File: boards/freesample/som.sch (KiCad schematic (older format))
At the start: 15 parts, among them J10 XILINX_JTAG, J19 JUMPER, J20 JUMPER, J21 JUMPER, J7 CONN_INTEGRALSTICK_FPGA_HOST, J8 CONN_INTEGRALSTICK_MCU_HOST, J9 0826-1G1T-23-F, Q1 SSM6N58NU

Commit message: Added more test points. Started picking packages for passives. Continued schematic review.
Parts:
- added J24, J25: SMA, azonenberg_pcb:CONN_SMA_EDGE_SAMTEC_SMA_J_P_H_ST_EM1, symbol Connector:Conn_Coaxial
- C129, C130, C131, C132, C321: footprint (none) -> azonenberg_pcb:EIA_0402_CAP_NOSILK
- J10: footprint (none) -> azonenberg_pcb:XILINX_JTAG_PTH_MOLEX_0878311420
- J7, J8: footprint (none) -> azonenberg_pcb:CONN_SAMTEC_QSH-060-01-L-D-A
- J9: footprint (none) -> azonenberg_pcb:CONN_BELFUSE_0826_1G1T_23_F
- Q1: footprint (none) -> azonenberg_pcb:DFN_6_0.65MM_2x2MM_GDS
- R16, R17: footprint (none) -> azonenberg_pcb:EIA_0402_RES_NOSILK
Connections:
- net GND: now also J24.2 (Ext), J25.2 (Ext)
- net SMA_GPIO_N: now reaches J7.10 (LVDS_DQ8_N)
- net SMA_GPIO_N: now also J25.1 (In)
- net SMA_GPIO_P: now reaches J7.12 (LVDS_DQ8_P)
- net SMA_GPIO_P: now also J24.1 (In)
- no-connect marks 88 -> 86

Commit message: Continued assigning footprints
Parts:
- J19, J20, J21: footprint (none) -> azonenberg_pcb:CONN_HEADER_2.54MM_1x2
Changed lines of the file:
@@
 Sheet 9 12
 Title "FREESAMPLE Oscilloscope"
-Date "2019-03-15"
+Date "2019-03-16"
 Rev "0.1"
 Comp "Andrew D. Zonenberg / Antikernel Labs"
@@
 F 0 "J19" H 10130 5642 50  0000 L CNN
 F 1 "JUMPER" H 10130 5551 50  0000 L CNN
-F 2 "" H 10050 5650 50  0001 C CNN
+F 2 "azonenberg_pcb:CONN_HEADER_2.54MM_1x2" H 10050 5650 50  0001 C CNN
 F 3 "~" H 10050 5650 50  0001 C CNN
 	1    10050 5650
@@
 F 0 "J20" H 10130 5992 50  0000 L CNN
 F 1 "JUMPER" H 10130 5901 50  0000 L CNN
-F 2 "" H 10050 6000 50  0001 C CNN
+F 2 "azonenberg_pcb:CONN_HEADER_2.54MM_1x2" H 10050 6000 50  0001 C CNN
 F 3 "~" H 10050 6000 50  0001 C CNN
 	1    10050 6000
@@
 F 0 "J21" H 10130 6292 50  0000 L CNN
 F 1 "JUMPER" H 10130 6201 50  0000 L CNN
-F 2 "" H 10050 6300 50  0001 C CNN
+F 2 "azonenberg_pcb:CONN_HEADER_2.54MM_1x2" H 10050 6300 50  0001 C CNN
 F 3 "~" H 10050 6300 50  0001 C CNN
 	1    10050 6300

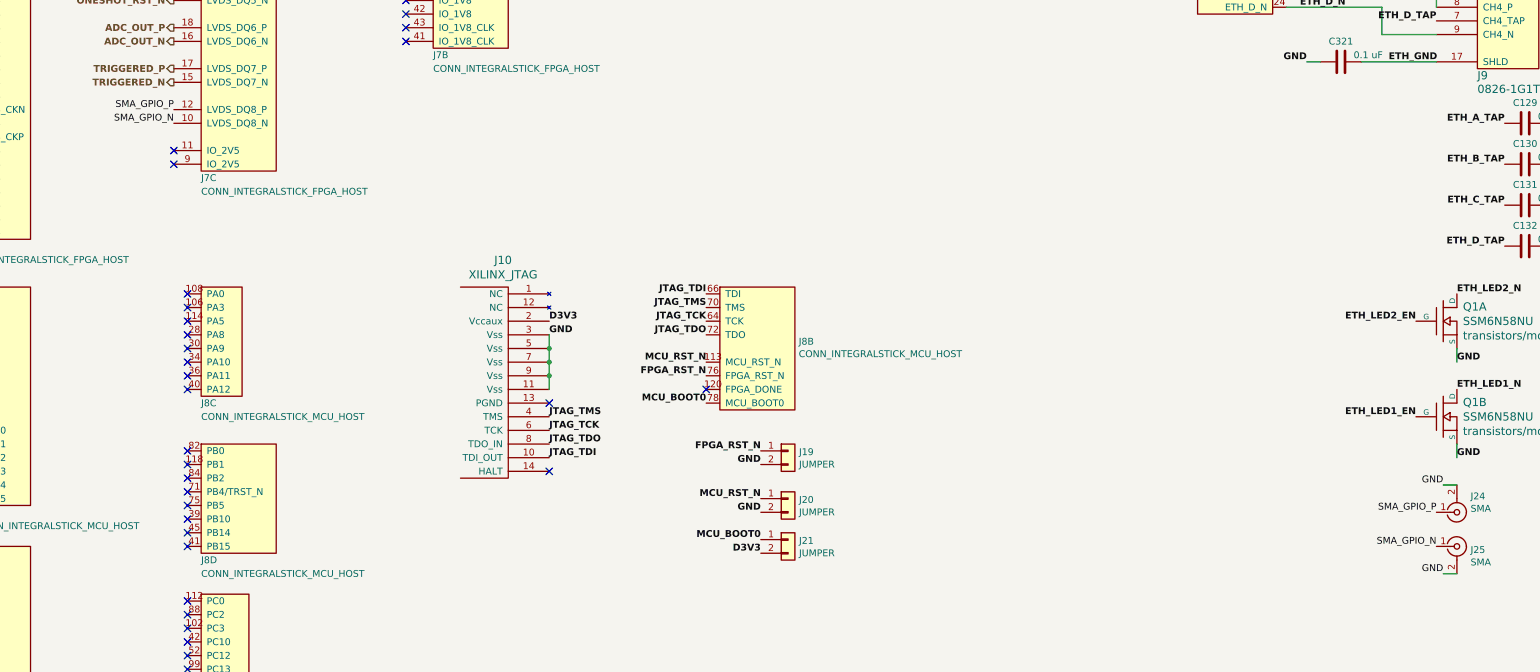
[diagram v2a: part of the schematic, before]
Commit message: Continued schematic review. Significantly simplified one-shot to reduce jitter, board area, and power consumption
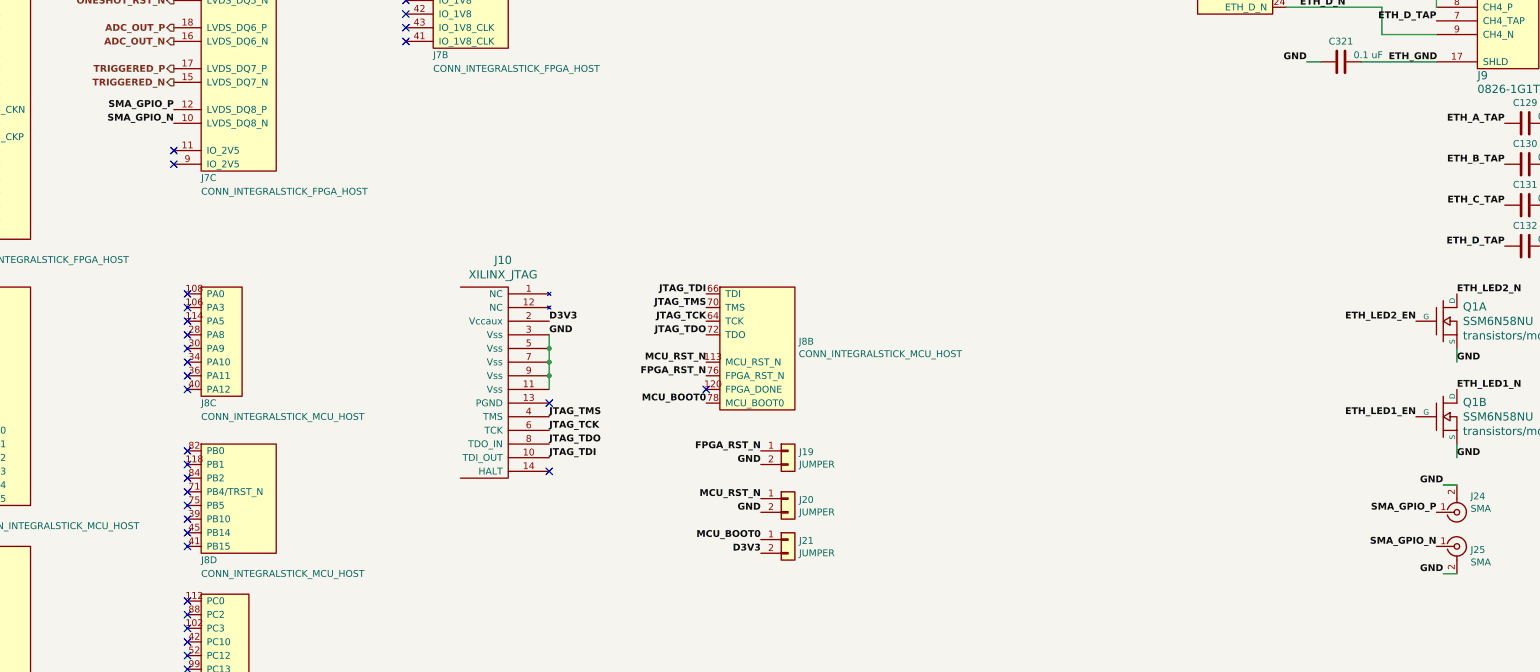
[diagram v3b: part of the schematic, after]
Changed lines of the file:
@@
 Text Label 9450 5300 2    50   ~ 6
 MCU_BOOT0
-Text Label 5550 3150 2    50   ~ 0
+Text Label 5550 3150 2    50   ~ 6
 SMA_GPIO_P
-Text Label 5550 3250 2    50   ~ 0
+Text Label 5550 3250 2    50   ~ 6
 SMA_GPIO_N
-Text Label 14800 6100 2    50   ~ 0
+Text Label 14800 6100 2    50   ~ 6
 SMA_GPIO_P
-Text Label 14800 6350 2    50   ~ 0
+Text Label 14800 6350 2    50   ~ 6
 SMA_GPIO_N
 $Comp
@@
 	1    0    0    -1
 $EndComp
-Text Label 14850 6550 2    50   ~ 0
+Text Label 14850 6550 2    50   ~ 6
 GND
 Wire Wire Line
 	14850 6550 14950 6550
-Text Label 14850 5900 2    50   ~ 0
+Text Label 14850 5900 2    50   ~ 6
 GND
 Wire Wire Line

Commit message: Finished schematic review. Added a bunch more test points. Need to make a few footprints then ready for layout!
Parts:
- added J26: PMOD_HOST, azonenberg_pcb:CONN_HEADER_2.54MM_2x6_RA_PMOD_HOST, symbol special-azonenberg:PMOD_HOST
- added TP32, TP33, TP34, TP35: GROUNDCLIP, azonenberg_pcb:TESTPOINT_SMT_KEYSTONE_5016, symbol Connector:Conn_01x01
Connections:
- net D3V3: now also J26.12 (3V3), J26.6 (3V3)
- net GND: now also J26.11 (GND), J26.5 (GND), TP32.1 (Pin_1), TP33.1 (Pin_1), TP34.1 (Pin_1), TP35.1 (Pin_1)
- net GPIO7: now reaches J7.104 (IO_3V3)
- net GPIO7: now also J26.10 (D7)
- net GPIO0: now reaches J7.110 (IO_3V3)
- net GPIO0: now also J26.1 (D0)
- net GPIO1: now reaches J7.113 (IO_3V3)
- net GPIO1: now also J26.2 (D1)
- net GPIO2: now reaches J7.114 (IO_3V3)
- net GPIO2: now also J26.3 (D2)
- net GPIO3: now reaches J7.115 (IO_3V3)
- net GPIO3: now also J26.4 (D3)
- net GPIO4: now reaches J7.116 (IO_3V3)
- net GPIO4: now also J26.7 (D4)
- net GPIO5: now reaches J7.119 (IO_3V3)
- net GPIO5: now also J26.8 (D5)
- net GPIO6: now reaches J7.120 (IO_3V3)
- net GPIO6: now also J26.9 (D6)
- no-connect marks 86 -> 78
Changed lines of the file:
@@
 	1    0    0    -1
 $EndComp
-NoConn ~ 3800 3050
 NoConn ~ 3800 3250
-NoConn ~ 3800 3450
-NoConn ~ 3800 3550
-NoConn ~ 3800 3650
-NoConn ~ 3800 3750
-NoConn ~ 3800 3850
-NoConn ~ 3800 3950
-NoConn ~ 3800 4050
 Text HLabel 3800 3350 0    50   Input ~ 6
 FPGA_CLK_P
@@
 Wire Wire Line
 	14850 5900 14950 5900
+$Comp
+L special-azonenberg:PMOD_HOST J26
+U 1 1 5D13EF9C
+P 9750 2650
+F 0 "J26" H 10128 3358 60  0000 L CNN
+F 1 "PMOD_HOST" H 10128 3252 60  0000 L CNN
+F 2 "azonenberg_pcb:CONN_HEADER_2.54MM_2x6_RA_PMOD_HOST" H 9750 2650 60  0001 C CNN
+F 3 "" H 9750 2650 60  0001 C CNN
+	1    9750 2650
+	1    0    0    -1
+$EndComp
+Text Label 9400 1400 2    50   ~ 0
+D3V3
+Wire Wire Line
+	9400 1400 9550 1400
+Wire Wire Line
+	9550 1400 9550 1500
+Connection ~ 9550 1400
+Text Label 9400 1600 2    50   ~ 0
+GND
+Wire Wire Line
+	9400 1600 9550 1600
+Wire Wire Line
+	9550 1600 9550 1700
+Connection ~ 9550 1600
+Text Label 9400 1900 2    50   ~ 0
+GPIO0
+Wire Wire Line
+	9400 1900 9550 1900
+Text Label 9400 2000 2    50   ~ 0
+GPIO1
+Text Label 9400 2100 2    50   ~ 0
+GPIO2
+Text Label 9400 2200 2    50   ~ 0
+GPIO3
+Wire Wire Line
+	9400 2200 9550 2200
+Wire Wire Line
+	9550 2100 9400 2100
+Wire Wire Line
+	9400 2000 9550 2000
+Text Label 3800 3450 2    50   ~ 0
+GPIO0
+Text Label 3800 3550 2    50   ~ 0
+GPIO1
+Text Label 3800 3650 2    50   ~ 0
+GPIO2
+Text Label 3800 3750 2    50   ~ 0
+GPIO3
+Text Label 3800 3850 2    50   ~ 0
+GPIO4
+Text Label 3800 3950 2    50   ~ 0
+GPIO5
+Text Label 3800 4050 2    50   ~ 0
+GPIO6
+Text Label 3800 3050 2    50   ~ 0
+GPIO7
+Text Label 9400 2300 2    50   ~ 0
+GPIO4
+Wire Wire Line
+	9400 2300 9550 2300
+Text Label 9400 2400 2    50   ~ 0
+GPIO5
+Text Label 9400 2500 2    50   ~ 0
+GPIO6
+Text Label 9400 2600 2    50   ~ 0
+GPIO7
+Wire Wire Line
+	9400 2600 9550 2600
+Wire Wire Line
+	9550 2500 9400 2500
+Wire Wire Line
+	9400 2400 9550 2400
+$Comp
+L Connector:Conn_01x01 TP32
+U 1 1 5D18E7AD
+P 11250 2050
+F 0 "TP32" H 11330 2092 50  0000 L CNN
+F 1 "GROUNDCLIP" H 11330 2001 50  0000 L CNN
+F 2 "azonenberg_pcb:TESTPOINT_SMT_KEYSTONE_5016" H 11250 2050 50  0001 C CNN
+F 3 "~" H 11250 2050 50  0001 C CNN
+	1    11250 2050
+	1    0    0    -1
+$EndComp
+Text Label 11050 2050 2    50   ~ 0
+GND
+$Comp
+L Connector:Conn_01x01 TP33
+U 1 1 5D190177
+P 11250 2300
+F 0 "TP33" H 11330 2342 50  0000 L CNN
+F 1 "GROUNDCLIP" H 11330 2251 50  0000 L CNN
+F 2 "azonenberg_pcb:TESTPOINT_SMT_KEYSTONE_5016" H 11250 2300 50  0001 C CNN
+F 3 "~" H 11250 2300 50  0001 C CNN
+	1    11250 2300
+	1    0    0    -1
+$EndComp
+Text Label 11050 2300 2    50   ~ 0
+GND
+$Comp
+L Connector:Conn_01x01 TP34
+U 1 1 5D198D70
+P 11250 2550
+F 0 "TP34" H 11330 2592 50  0000 L CNN
+F 1 "GROUNDCLIP" H 11330 2501 50  0000 L CNN
+F 2 "azonenberg_pcb:TESTPOINT_SMT_KEYSTONE_5016" H 11250 2550 50  0001 C CNN
+F 3 "~" H 11250 2550 50  0001 C CNN
+	1    11250 2550
+	1    0    0    -1
+$EndComp
+Text Label 11050 2550 2    50   ~ 0
+GND
+$Comp
+L Connector:Conn_01x01 TP35
+U 1 1 5D198D7B
+P 11250 2800
+F 0 "TP35" H 11330 2842 50  0000 L CNN
+F 1 "GROUNDCLIP" H 11330 2751 50  0000 L CNN
+F 2 "azonenberg_pcb:TESTPOINT_SMT_KEYSTONE_5016" H 11250 2800 50  0001 C CNN
+F 3 "~" H 11250 2800 50  0001 C CNN
+	1    11250 2800
+	1    0    0    -1
+$EndComp
+Text Label 11050 2800 2    50   ~ 0
+GND
 $EndSCHEMATC

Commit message: Added fiducials
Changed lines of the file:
@@
 	1    0    0    -1
 $EndComp
-Text Label 9400 1400 2    50   ~ 0
+Text Label 9400 1400 2    50   ~ 6
 D3V3
 Wire Wire Line
@@
 	9550 1400 9550 1500
 Connection ~ 9550 1400
-Text Label 9400 1600 2    50   ~ 0
+Text Label 9400 1600 2    50   ~ 6
 GND
 Wire Wire Line
@@
 	9550 1600 9550 1700
 Connection ~ 9550 1600
-Text Label 9400 1900 2    50   ~ 0
+Text Label 9400 1900 2    50   ~ 6
 GPIO0
 Wire Wire Line
 	9400 1900 9550 1900
-Text Label 9400 2000 2    50   ~ 0
+Text Label 9400 2000 2    50   ~ 6
 GPIO1
-Text Label 9400 2100 2    50   ~ 0
+Text Label 9400 2100 2    50   ~ 6
 GPIO2
-Text Label 9400 2200 2    50   ~ 0
+Text Label 9400 2200 2    50   ~ 6
 GPIO3
 Wire Wire Line
@@
 Wire Wire Line
 	9400 2000 9550 2000
-Text Label 3800 3450 2    50   ~ 0
+Text Label 3800 3450 2    50   ~ 6
 GPIO0
-Text Label 3800 3550 2    50   ~ 0
+Text Label 3800 3550 2    50   ~ 6
 GPIO1
-Text Label 3800 3650 2    50   ~ 0
+Text Label 3800 3650 2    50   ~ 6
 GPIO2
-Text Label 3800 3750 2    50   ~ 0
+Text Label 3800 3750 2    50   ~ 6
 GPIO3
-Text Label 3800 3850 2    50   ~ 0
+Text Label 3800 3850 2    50   ~ 6
 GPIO4
-Text Label 3800 3950 2    50   ~ 0
+Text Label 3800 3950 2    50   ~ 6
 GPIO5
-Text Label 3800 4050 2    50   ~ 0
+Text Label 3800 4050 2    50   ~ 6
 GPIO6
-Text Label 3800 3050 2    50   ~ 0
+Text Label 3800 3050 2    50   ~ 6
 GPIO7
-Text Label 9400 2300 2    50   ~ 0
+Text Label 9400 2300 2    50   ~ 6
 GPIO4
 Wire Wire Line
 	9400 2300 9550 2300
-Text Label 9400 2400 2    50   ~ 0
+Text Label 9400 2400 2    50   ~ 6
 GPIO5
-Text Label 9400 2500 2    50   ~ 0
+Text Label 9400 2500 2    50   ~ 6
 GPIO6
-Text Label 9400 2600 2    50   ~ 0
+Text Label 9400 2600 2    50   ~ 6
 GPIO7
 Wire Wire Line
@@
 	1    0    0    -1
 $EndComp
-Text Label 11050 2050 2    50   ~ 0
+Text Label 11050 2050 2    50   ~ 6
 GND
 $Comp
@@
 	1    0    0    -1
 $EndComp
-Text Label 11050 2300 2    50   ~ 0
+Text Label 11050 2300 2    50   ~ 6
 GND
 $Comp
@@
 	1    0    0    -1
 $EndComp
-Text Label 11050 2550 2    50   ~ 0
+Text Label 11050 2550 2    50   ~ 6
 GND
 $Comp
@@
 	1    0    0    -1
 $EndComp
-Text Label 11050 2800 2    50   ~ 0
+Text Label 11050 2800 2    50   ~ 6
 GND
 $EndSCHEMATC
